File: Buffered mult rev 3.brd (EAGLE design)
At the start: 100.3 x 17.1 mm, 28 parts, among them IC1 OPA4171, IC2 OPA2171, J1 EURO_POWER_HEADERFAT_PADS

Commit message: minor changes
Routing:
- net GND: track 158.0 -> 140.2 mm, vias 11 -> 1
- net N$15: track 30.7 -> 23.8 mm, vias 3 -> 0
- net N$14: track 21.0 -> 14.1 mm, vias 3 -> 0
- net VEE: track 77.3 -> 78.9 mm
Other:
- board text added: "༼ ͒ ̶ ͒༽"
- board text added: "༼ ͒ ͓ ͒༽"
- board text added: "ヽ(°◇° )ノ"
- board text removed: "PASS DAT SHIT"

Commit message: Layout done.
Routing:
- net GND: track 140.2 -> 143.3 mm
- net VEE: track 78.9 -> 79.5 mm
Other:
- board size 100.3 x 17.1 mm -> 100.4 x 17.6 mm
- board text added: "Gilberte / Mads Kjeldgaard"
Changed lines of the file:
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@@
 <board>
 <plain>
-<wire x1="100.2" y1="0" x2="99.97" y2="17.05" width="0" layer="20"/>
-<wire x1="99.97" y1="17.05" x2="-0.1" y2="17.05" width="0" layer="20"/>
-<wire x1="-0.1" y1="17.05" x2="0" y2="0.1" width="0" layer="20"/>
-<wire x1="0" y1="0.1" x2="100.2" y2="0" width="0" layer="20"/>
+<wire x1="100.2" y1="-0.2" x2="100.27" y2="17.45" width="0" layer="20"/>
+<wire x1="100.27" y1="17.45" x2="-0.1" y2="17.35" width="0" layer="20"/>
+<wire x1="-0.1" y1="17.35" x2="0" y2="0" width="0" layer="20"/>
 <text x="96.9" y="5.5" size="1.778" layer="26" rot="MR0">༼ ͒ ̶ ͒༽</text>
 <text x="56.7" y="0.7" size="1.778" layer="26" rot="MR0">༼ ͒ ͓ ͒༽</text>
@@
 <text x="84.3" y="5" size="1.778" layer="26" rot="MR0">༼ ͒ ̶ ͒༽</text>
 <text x="65.7" y="8" size="1.778" layer="26" rot="MR0">༼ ͒ ̶ ͒༽</text>
-<wire x1="0" y1="0.1" x2="100.2" y2="0" width="0" layer="20"/>
+<wire x1="0" y1="0" x2="100.2" y2="-0.2" width="0" layer="20"/>
 <text x="34.2" y="8.7" size="1.778" layer="26" rot="MR0">༼ ͒ ͓ ͒༽</text>
+<text x="34.9" y="20.2" size="1.778" layer="25">Gilberte / Mads Kjeldgaard</text>
 </plain>
 <attributes>
@@
 <wire x1="35.8902" y1="1.8288" x2="35.7" y2="1.9" width="0.254" layer="16"/>
 <wire x1="55.3212" y1="5.715" x2="55.3212" y2="7.0866" width="0.254" layer="16"/>
-<wire x1="58.9788" y1="2.0574" x2="55.3212" y2="5.715" width="0.254" layer="16"/>
+<wire x1="57.5788" y1="4.0574" x2="55.3212" y2="5.715" width="0.254" layer="16"/>
 <wire x1="55.3212" y1="7.0866" x2="55.2" y2="7.2" width="0.254" layer="16"/>
-<wire x1="58.9788" y1="2.0574" x2="59" y2="1.9" width="0.254" layer="16"/>
+<wire x1="57.5788" y1="4.0574" x2="59" y2="1.9" width="0.254" layer="16"/>
 <wire x1="51.6636" y1="2.0574" x2="47.3202" y2="2.0574" width="0.254" layer="16"/>
 <wire x1="55.3212" y1="5.715" x2="51.6636" y2="2.0574" width="0.254" layer="16"/>
@@
 <wire x1="35.8902" y1="1.8288" x2="35.7" y2="1.9" width="0.254" layer="1"/>
 <wire x1="47.0916" y1="1.8288" x2="47.1" y2="1.9" width="0.254" layer="1"/>
-<wire x1="59.2074" y1="2.0574" x2="70.4088" y2="2.0574" width="0.254" layer="1"/>
+<wire x1="59.2074" y1="4.5574" x2="70.4088" y2="2.0574" width="0.254" layer="1"/>
 <wire x1="70.4088" y1="2.0574" x2="70.6" y2="2" width="0.254" layer="1"/>
-<wire x1="59.2074" y1="2.0574" x2="59" y2="1.9" width="0.254" layer="1"/>
+<wire x1="59.2074" y1="4.5574" x2="59" y2="1.9" width="0.254" layer="1"/>
 <wire x1="34.7472" y1="2.0574" x2="24.2316" y2="2.0574" width="0.254" layer="16"/>
 <wire x1="35.2044" y1="2.5146" x2="34.7472" y2="2.0574" width="0.254" layer="16"/>
@@
 <wire x1="6.4008" y1="6.858" x2="6.37" y2="6.96" width="0.254" layer="1"/>
 <wire x1="13.0302" y1="2.0574" x2="13.1" y2="2" width="0.254" layer="1"/>
-<via x="59.2074" y="2.0574" extent="1-16" drill="0.6" shape="square"/>
-<wire x1="59.2074" y1="2.0574" x2="59.1" y2="2.0574" width="0.4064" layer="16"/>
-<wire x1="59.1" y1="2.0574" x2="59.1" y2="0.5" width="0.4064" layer="16"/>
-<wire x1="59.1" y1="0.5" x2="62.41" y2="0.5" width="0.4064" layer="16"/>
+<via x="59.2074" y="4.5574" extent="1-16" drill="0.6" shape="square"/>
+<wire x1="59.2074" y1="4.5574" x2="59.2426" y2="4.6" width="0.4064" layer="16"/>
+<wire x1="59.2426" y1="4.6" x2="61.5" y2="2.5" width="0.4064" layer="16"/>
+<wire x1="61.5" y1="2.5" x2="62.41" y2="0.5" width="0.4064" layer="16"/>
 <wire x1="62.41" y1="0.5" x2="62.41" y2="1.12" width="0.4064" layer="16"/>
 <wire x1="62.41" y1="1.12" x2="64.83" y2="1.12" width="0.4064" layer="16"/>
@@
 <wire x1="42.0624" y1="3.6576" x2="42.0624" y2="4.1148" width="0.254" layer="16"/>
 <wire x1="42.5196" y1="3.2004" x2="42.0624" y2="3.6576" width="0.254" layer="16"/>
-<wire x1="43.6626" y1="3.2004" x2="42.5196" y2="3.2004" width="0.254" layer="16"/>
-<wire x1="45.0912" y1="4.0718" x2="43.6626" y2="3.2004" width="0.254" layer="16"/>
+<wire x1="44.1626" y1="2.7004" x2="42.5196" y2="3.2004" width="0.254" layer="16"/>
+<wire x1="45.0912" y1="4.0718" x2="44.1626" y2="2.7004" width="0.254" layer="16"/>
 <wire x1="40.2336" y1="2.9718" x2="45.0912" y2="4.0718" width="0.254" layer="1"/>
 <wire x1="38.6192" y1="3.2862" x2="40.2336" y2="2.9718" width="0.254" layer="1"/>

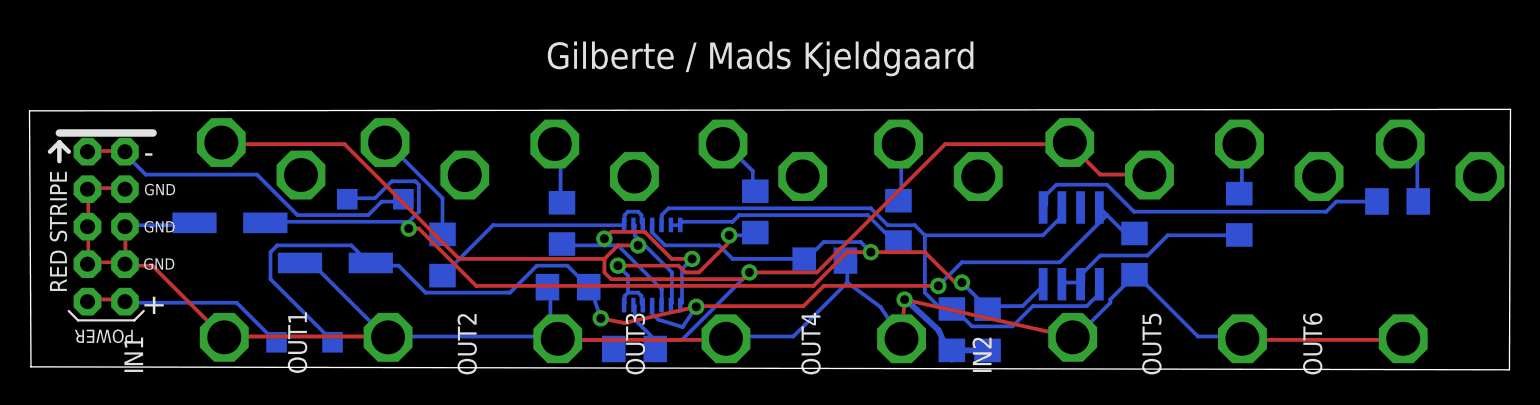
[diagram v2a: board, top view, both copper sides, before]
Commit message: Finalized design, generated Gerbers.
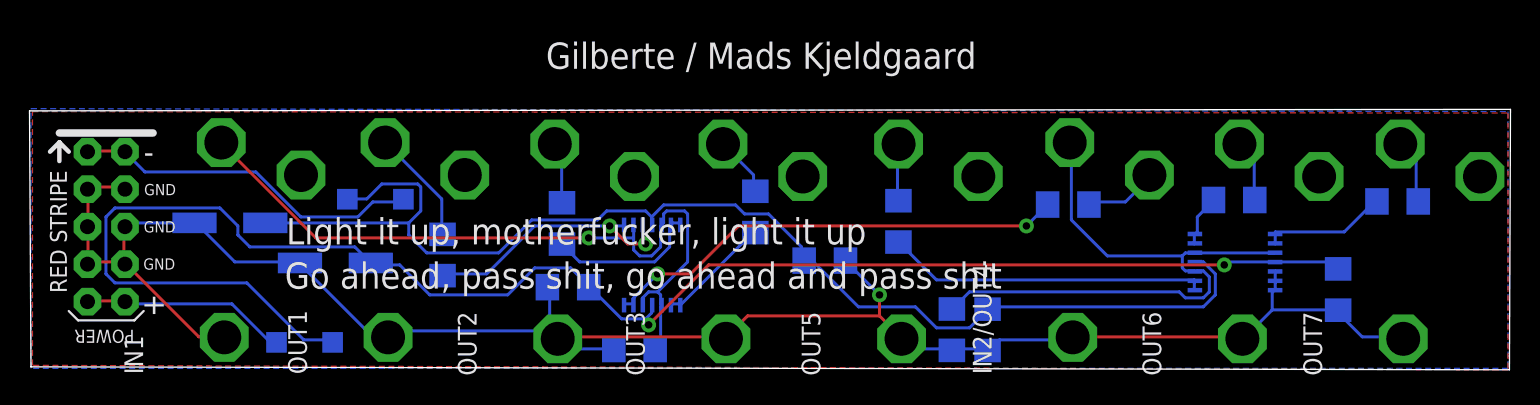
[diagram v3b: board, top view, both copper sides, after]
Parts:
- removed IC2: OPA2171, linear:SO08
- removed OUT4: PJ302M, pj302m:PJ302M
- added IC3: OPA4171, linear:TSSOP14
- added OUT7: PJ302M, pj302m:PJ302M
- added R9: 1k, SparkFun-Passives:1206
- moved OUT5 23.1 mm to (59.0, -0.60)
- moved C3 14.0 mm to (88.6, 5.24)
- moved OUT6 10.9 mm to (82.1, -0.60)
- moved R5 1.03 mm to (81.5, 11.3), turned to 180 degrees
- renumbered IN2 to IN2/OUT4
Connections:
- removed net N$11: IC1.5, IC2.2, IC2.5, R8.2
- new net N$16: IC1.13, IC1.14, R9.1
- new net N$18: IN2/OUT4.SW, R9.2
- new net N$19: IC3.10, IC3.3, IC3.5, IN2/OUT4.TIP, R8.2
- net GND: now also IC3.12, IC3.13, IC3.14, OUT7.GND; no longer OUT4.GND
- net N$1: now also OUT7.TIP; no longer OUT6.TIP
- net N$10: now also IC1.6, IC1.7; no longer IC1.10, IC1.8
- net N$12: now also IC3.8, IC3.9; no longer IC2.1
- net N$13: now also IC3.6, IC3.7; no longer IC2.6, IC2.7
- net N$17: now also IC3.1, IC3.2; no longer IC1.6, IC1.7
- net N$3: now also OUT6.TIP; no longer OUT5.TIP
- net N$4: now also OUT5.TIP; no longer OUT4.TIP
- net N$5: now also IC1.10, IC1.12, IC1.5; no longer IC1.13, IC1.9, IN2/OUT4.SW, IN2/OUT4.TIP
- net N$6: now also IC1.8, IC1.9; no longer IC1.12, IC1.14
- net VCC: now also IC3.4; no longer IC2.8
- net VEE: now also IC3.11; no longer IC2.4
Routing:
- net N$11: track 48.2 -> 0.00 mm
- net N$5: track 93.9 -> 50.7 mm, vias 2 -> 1
- net N$19: track 0.00 -> 42.4 mm
- net VEE: track 79.5 -> 113.4 mm, vias 3 -> 2
- net N$16: track 0.00 -> 31.9 mm, vias 0 -> 2
- net N$12: track 24.7 -> 8.59 mm
- net GND: track 143.3 -> 131.5 mm
- net N$13: track 13.9 -> 3.56 mm
- net N$10: track 19.9 -> 10.5 mm, vias 2 -> 0
- net N$6: track 15.6 -> 7.84 mm, vias 2 -> 0
- net N$17: track 16.6 -> 21.8 mm
- net N$18: track 0.00 -> 5.11 mm
- net N$2: track 16.5 -> 18.1 mm, vias 0 -> 2
- net VCC: track 83.4 -> 84.2 mm, vias 3 -> 0
- net N$3: track 3.60 -> 4.27 mm
- added copper zone on layer 16, net N$11
- added copper zone on layer 1, net N$20
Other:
- board text added: "Go ahead, pass shit, go ahead and pass shit"
- board text added: "Light it up, motherfucker, light it up"
